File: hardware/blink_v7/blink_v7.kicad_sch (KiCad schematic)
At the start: 104 parts, among them J1 Conn_01x02, J14 Conn_02x16_Odd_Even, J5 Conn_01x04_Pin, J6 Conn_01x04_Pin, J7 Conn_01x06_Pin, J8 Conn_01x06, J9 USB_C_Receptacle, SW1 MK-12C02-G025, SW2 LC1258OASP, SW3 LC1258OASP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

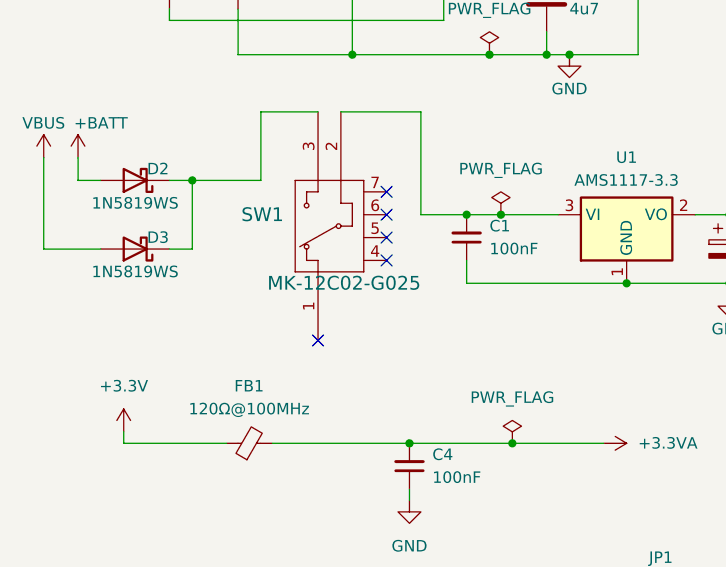
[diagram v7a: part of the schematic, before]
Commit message: update slide switch
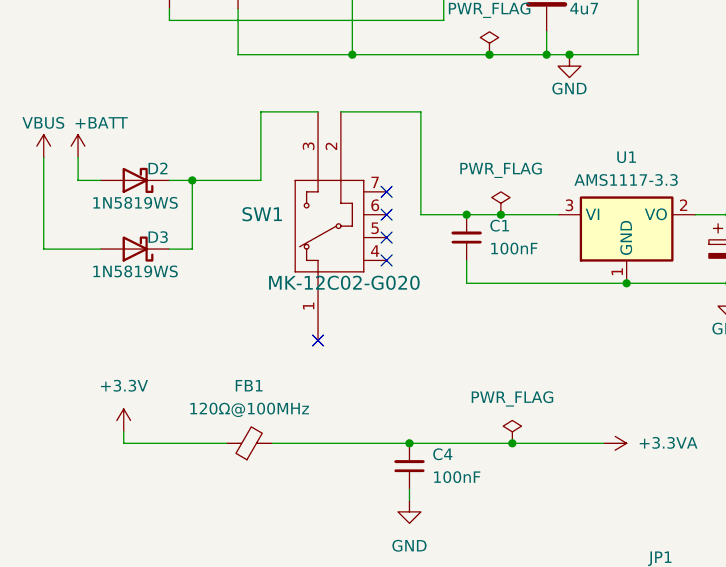
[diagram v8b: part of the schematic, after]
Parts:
- SW1: value MK-12C02-G025 -> MK-12C02-G020; JLCPCB Part # C778186 -> C963206
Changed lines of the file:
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@@
       (effects (font (size 1.524 1.524)) (justify left))
     )
-    (property "Value" "MK-12C02-G025" (at 58.42 71.12 90)
+    (property "Value" "MK-12C02-G020" (at 58.42 71.12 90)
       (effects (font (size 1.524 1.524)) (justify left))
     )
@@
       (effects (font (size 1.27 1.27) italic) hide)
     )
-    (property "JLCPCB Part #" "C778186" (at 46.99 77.47 0)
+    (property "JLCPCB Part #" "C963206" (at 46.99 77.47 0)
       (effects (font (size 1.27 1.27)) hide)
     )
